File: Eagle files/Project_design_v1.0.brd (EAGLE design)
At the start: 57.5 x 43.2 mm, 64 parts, among them CN1 USB_CONN, CN2 BATT_IN_JST, IC1 TPS73233DBVT, IC2 TPS73233DBVT, IC3 MCP73833T-AMI/MF, IC4 STM32F042K6T6, IC5 MCP9700T-E/TT, IC6 TLV379IDBVT, Q1 PMV16XN, Q2 PMV16XN, Q3 PMV16XN, Q4 PMV16XN

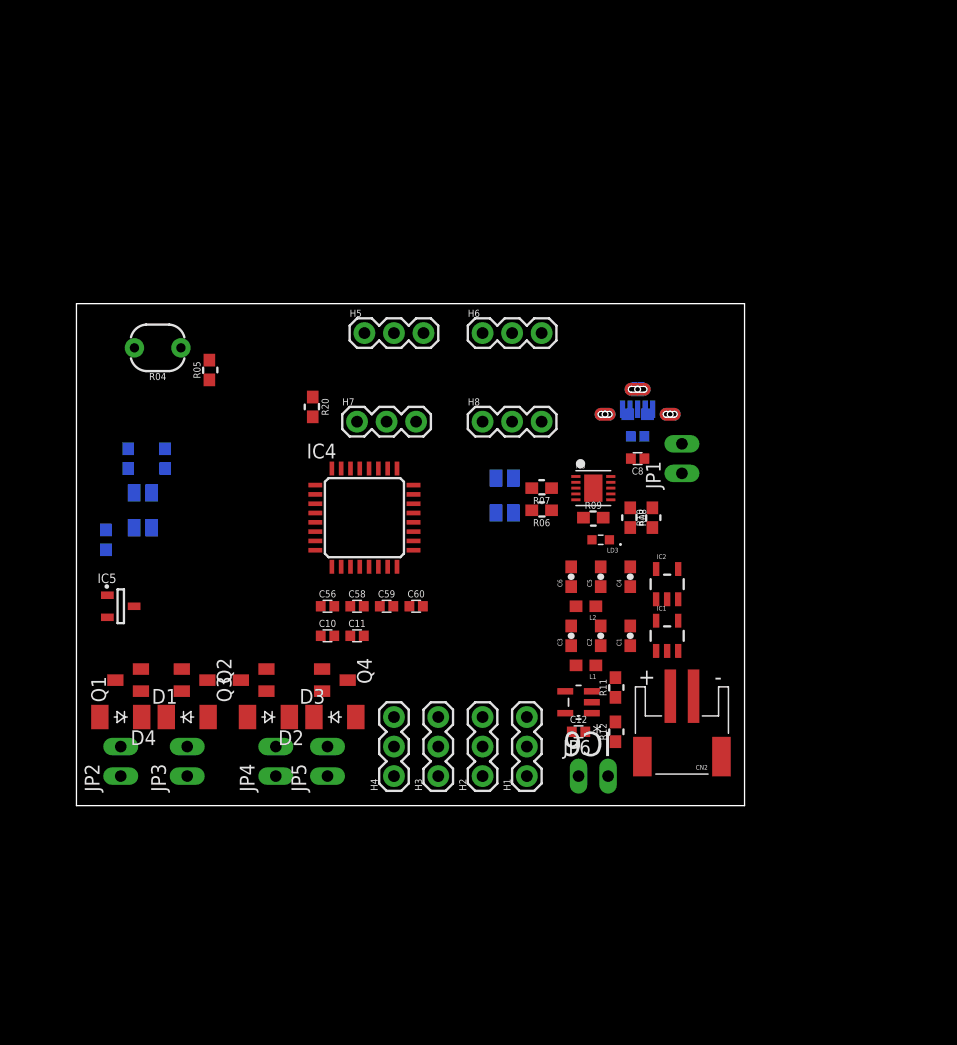
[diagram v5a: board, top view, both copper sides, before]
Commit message: schematic almose finished, part number edited, and PIR & buzzer added
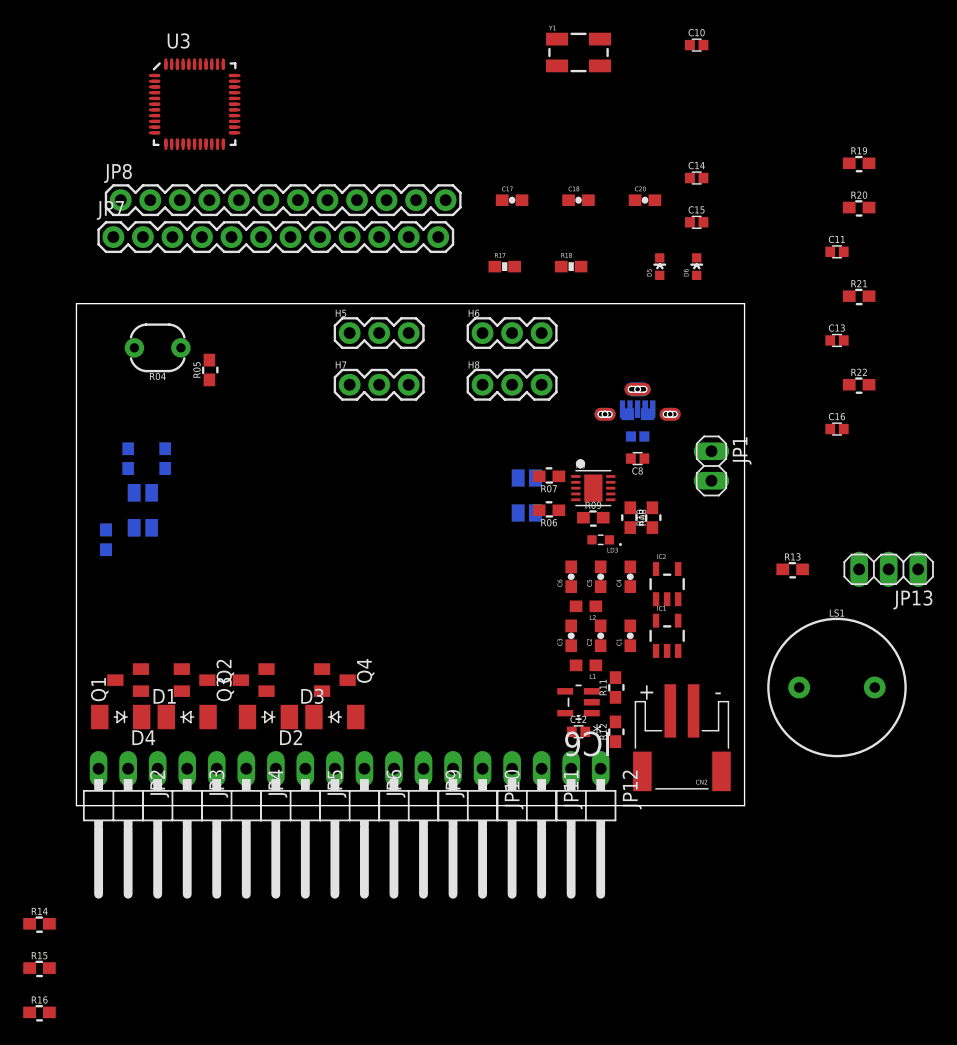
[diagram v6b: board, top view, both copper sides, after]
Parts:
- removed C56, C58, C59, C60: 100n, custom_part:0402
- removed H1, H2, H3, H4: SOIL_MOISTURE, potentiometer:SOIL_MOISTURE
- removed IC4: STM32F042K6T6, stm32-microcontrollers:LQFP32-7X7
- removed IC5: MCP9700T-E/TT, MCP9700T-E_TT:SOT95P237X112-3N
- added C13, C14, C15, C16: 100n, custom_part:0402
- added C17, C18: 22pF, SparkFun:0603-CAP
- added C20: 1uF, SparkFun:0603-CAP
- added D5: Green, SparkFun:LED-0603
- added D6: Yellow, SparkFun:LED-0603
- added JP10, JP11, JP12, JP9: Connectors, pinhead:1X02/90
- added JP13: PIN-1X3, pinhead:1X03
- added JP7, JP8: (no value), SparkFun:1X12
- added LS1: BUZZER-PTH_KIT, SparkFun-Electromechanical:BUZZER-12MM-KIT
- added R13, R15, R16: 330, custom_part:0603
- added R14, R19, R21, R22: 10k, custom_part:0603
- added R17, R18: 22, SparkFun:0603-RES
- added U3: ATMEGA32U4, Testing:QFN-44-NOPAD_1:1-OUTFAKES
- added Y1: 16MHz, SparkFun:CRYSTAL-SMD-5X3
- JP1: value Contact_pin -> Connectors; device microbuilder:1X02_OVAL -> pinhead:1X02
- JP2, JP3, JP4, JP5, JP6: value Contact_pin -> Connectors; device microbuilder:1X02_OVAL -> pinhead:1X02/90
- R06, R07, R08: value 221 -> 330
- R11, R12: value 221 -> 10k
- moved C10 59.9 mm to (53.3, 65.4)
- moved C11 52.9 mm to (65.4, 47.6)
- moved R20 50.0 mm to (67.3, 51.4), turned to 0 degrees
- moved JP6 21.2 mm to (23.5, -0.64), turned to 180 degrees
- moved JP4 5.85 mm to (13.3, -0.64), turned to 180 degrees
- moved JP5 5.46 mm to (18.4, -0.64), turned to 180 degrees
- moved JP3 4.62 mm to (8.26, -0.64), turned to 180 degrees
- moved JP2 4.49 mm to (3.17, -0.64), turned to 180 degrees
- moved H7 3.24 mm to (26.0, 36.2)
- moved H8 3.17 mm to (37.5, 36.2)
- moved JP1 2.62 mm to (54.6, 29.2), turned to 270 degrees
- moved LD2 1.91 mm to (38.7, 26.7)
- moved CN2 1.27 mm to (52.1, 4.45)
- moved H5 1.27 mm to (26.0, 40.6)
- moved R07 1.20 mm to (40.6, 28.3)
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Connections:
- removed net BOOT0: IC4.31, R20.2
- removed net CHARGE_CMD: IC4.11
- removed net CTRL_MOIST1: H1.1
- removed net CTRL_MOIST2: H2.1
- removed net CTRL_MOIST3: H3.1
- removed net CTRL_MOIST4: H4.1
- removed net DAC_CLK: IC4.12
- removed net DAC_D2: IC4.13
- removed net DAC_D3: IC4.18
- removed net DAC_D4: IC4.19
- removed net DAC_D5: IC4.20
- removed net DAC_D6: IC4.21
- removed net DAC_D7: IC4.22
- removed net DAC_D8: IC4.25
- removed net HV_DONE: IC4.10
- removed net LI_PRESET: IC4.2
- removed net LOAD_CURRENT_1: IC4.6
- removed net LOAD_CURRENT_2: IC4.7
- removed net LOAD_CURRENT_3: IC4.8
- removed net LOAD_CURRENT_4: IC4.9
- removed net MUX_DIS: IC4.28
- removed net MUX_IN: IC4.14
- removed net MUX_S0: IC4.15
- removed net MUX_S1: IC4.26
- removed net MUX_S2: IC4.27
- removed net NRST: C59.1, IC4.4
- removed net SWCLK: IC4.24
- removed net SWDIO: IC4.23
- removed net TEMP_READ: IC5.2
- removed net USART1_RX/I2C1_SDA: IC4.30
- removed net USART1_TX/I2C1_SCL: IC4.29
- new net A0: JP7.8, U3.36
- new net A1: JP7.7, U3.37
- new net A2: JP7.6, U3.38
- new net A3: JP7.5, U3.39
- new net A4: U3.40
- new net A5: U3.41
- new net ALARM: JP13.3
- new net AREF: U3.42
- new net BUZZ: LS1.+
- new net D+: R17.1, U3.4
- new net D-: R18.1, U3.3
- new net D10: JP7.12, U3.30
- new net D11: U3.12
- new net D12: U3.26
- new net D13: U3.32
- new net D14: U3.8
- new net D2: JP8.8, U3.19
- new net D3: JP8.7, U3.18
- new net D4: JP8.6, U3.25
- new net D5: JP8.5, U3.31
- new net D6: JP8.4, U3.27
- new net D7: JP8.3, U3.1
- new net D8: JP8.2, U3.28
- new net D9: JP8.1, U3.29
- new net MISO: JP7.10, U3.11
- new net MOSI: JP7.11, U3.10
- new net N$18: C17.1, U3.17, Y1.3
- new net N$19: C20.2, U3.6
- new net N$20: CN1.2, R18.2
- new net N$21: CN1.3, R17.2
- new net N$22: LS1.-, R13.1
- new net N$23: D6.C
- new net N$24: D5.C
- new net N$9: C18.1, U3.16, Y1.1
- new net RESET: JP7.3, U3.13
- new net RXI: JP8.11, U3.20
- new net SCK: JP7.9, U3.9
- new net TXLED: U3.22
- new net TXO: JP8.12, U3.21
- net 3.3V: now also JP13.1, R19.2, R20.2, R21.2, R22.2, U3.14, U3.24, U3.34, U3.44; no longer C10.1, C11.1, C56.1, C58.1, IC4.1, IC4.17, IC5.1
- net 5.0V: now also U3.2, U3.7
- net GND: now also C13.2, C15.2, C16.2, C17.2, C18.2, C20.1, JP10.2, JP11.2, JP12.2, JP13.2, JP7.1, JP7.2, JP8.10, JP8.9, JP9.2, R13.2, U3.15, U3.23, U3.33, U3.35, U3.43, U3.5; no longer C10.2, C56.2, C58.2, C59.2, C60.2, H1.2, H2.2, H3.2, H4.2, IC4.16, IC4.32, IC5.3, R20.1
- net LED_G: no longer IC4.3
- net LEVEL_SENSOR: now also JP12.1; no longer JP6.1
- net MOISTURE1: now also C15.1, JP6.1, R19.1; no longer H1.3
- net MOISTURE2: now also C11.1, JP9.1, R20.1; no longer H2.3
- net MOISTURE3: now also C13.1, JP11.1, R21.1; no longer H3.3
- net MOISTURE4: now also C16.1, JP10.1, R22.1; no longer H4.3
- net VCC: now also D5.A, D6.A, JP7.4; no longer C60.1, IC4.5

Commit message: schematics design uptaded and adjusted for exportation for the MS2
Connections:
- net 3.3V: now also C10.1, R14.2
- net GND: now also C10.2
- net RESET: now also R14.1
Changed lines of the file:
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@@
 <contactref element="U3" pad="24"/>
 <contactref element="U3" pad="44"/>
+<contactref element="R14" pad="2"/>
+<contactref element="C10" pad="1"/>
 <wire x1="68.16" y1="51.435" x2="68.16" y2="55.245" width="0" layer="19" extent="1-1"/>
 <wire x1="68.16" y1="43.815" x2="68.16" y2="51.435" width="0" layer="19" extent="1-1"/>
 <wire x1="68.16" y1="36.195" x2="68.16" y2="43.815" width="0" layer="19" extent="1-1"/>
 <wire x1="72.39" y1="20.32" x2="68.16" y2="36.195" width="0" layer="19" extent="1-1"/>
+<wire x1="52.76" y1="65.405" x2="68.16" y2="55.245" width="0" layer="19" extent="1-1"/>
 <wire x1="42.965" y1="17.145" x2="72.39" y2="20.32" width="0" layer="19" extent="1-1"/>
 <wire x1="42.545" y1="18.835" x2="42.965" y2="17.145" width="0" layer="19" extent="1-1"/>
@@
 <wire x1="7.695" y1="63.6615" x2="12.625" y2="63.6615" width="0" layer="19" extent="1-1"/>
 <wire x1="6.465" y1="23.9" x2="23.495" y2="36.195" width="0" layer="19" extent="16-16"/>
+<wire x1="-2.325" y1="-10.16" x2="6.465" y2="23.9" width="0" layer="19" extent="1-16"/>
 </signal>
 <signal name="N$34">
@@
 <contactref element="JP11" pad="2"/>
 <contactref element="JP7" pad="1"/>
-<wire x1="65.985" y1="40.005" x2="65.985" y2="47.625" width="0" layer="19" extent="1-1"/>
-<wire x1="65.985" y1="32.385" x2="65.985" y2="40.005" width="0" layer="19" extent="1-1"/>
-<wire x1="54.61" y1="30.48" x2="65.985" y2="32.385" width="0" layer="19" extent="1-1"/>
-<wire x1="51.82" y1="33.655" x2="54.61" y2="30.48" width="0" layer="19" extent="16-16"/>
-<wire x1="49.56" y1="34.095" x2="51.82" y2="33.655" width="0" layer="19" extent="16-16"/>
-<wire x1="49.24" y1="35.795" x2="49.56" y2="34.095" width="0" layer="19" extent="16-16"/>
-<wire x1="47.41" y1="33.655" x2="49.56" y2="34.095" width="0" layer="19" extent="16-16"/>
-<wire x1="46.17" y1="33.655" x2="47.41" y2="33.655" width="0" layer="19" extent="16-16"/>
+<contactref element="C10" pad="2"/>
+<wire x1="48.045" y1="52.07" x2="53.92" y2="65.405" width="0" layer="19" extent="1-1"/>
+<wire x1="44.03" y1="52.07" x2="48.045" y2="52.07" width="0" layer="19" extent="1-1"/>
+<wire x1="38.315" y1="52.07" x2="44.03" y2="52.07" width="0" layer="19" extent="1-1"/>
+<wire x1="53.92" y1="50.165" x2="48.045" y2="52.07" width="0" layer="19" extent="1-1"/>
+<wire x1="37.465" y1="40.64" x2="38.315" y2="52.07" width="0" layer="19" extent="1-1"/>
+<wire x1="37.465" y1="36.195" x2="37.465" y2="40.64" width="0" layer="19" extent="1-1"/>
+<wire x1="46.17" y1="33.655" x2="37.465" y2="36.195" width="0" layer="19" extent="16-16"/>
+<wire x1="47.41" y1="33.655" x2="46.17" y2="33.655" width="0" layer="19" extent="16-16"/>
 <wire x1="47.68" y1="31.75" x2="47.41" y2="33.655" width="0" layer="19" extent="16-16"/>
 <wire x1="47.68" y1="29.845" x2="47.68" y2="31.75" width="0" layer="19" extent="1-16"/>
+<wire x1="49.56" y1="34.095" x2="47.41" y2="33.655" width="0" layer="19" extent="16-16"/>
+<wire x1="49.24" y1="35.795" x2="49.56" y2="34.095" width="0" layer="19" extent="16-16"/>
+<wire x1="51.82" y1="33.655" x2="49.56" y2="34.095" width="0" layer="19" extent="16-16"/>
+<wire x1="54.61" y1="30.48" x2="51.82" y2="33.655" width="0" layer="19" extent="16-16"/>
 <wire x1="42.95" y1="26.305" x2="47.68" y2="29.845" width="0" layer="19" extent="1-1"/>
 <wire x1="43.6" y1="24.765" x2="42.95" y2="26.305" width="0" layer="19" extent="1-1"/>
@@
 <wire x1="9.06" y1="9.845" x2="16.34" y2="11.745" width="0" layer="19" extent="1-1"/>
 <wire x1="5.545" y1="11.745" x2="9.06" y2="9.845" width="0" layer="19" extent="1-1"/>
-<wire x1="37.465" y1="36.195" x2="46.17" y2="33.655" width="0" layer="19" extent="16-16"/>
-<wire x1="37.465" y1="40.64" x2="37.465" y2="36.195" width="0" layer="19" extent="1-1"/>
 <wire x1="26.035" y1="40.64" x2="37.465" y2="40.64" width="0" layer="19" extent="1-1"/>
 <wire x1="26.035" y1="36.195" x2="26.035" y2="40.64" width="0" layer="19" extent="1-1"/>
-<wire x1="38.315" y1="52.07" x2="37.465" y2="40.64" width="0" layer="19" extent="1-1"/>
-<wire x1="44.03" y1="52.07" x2="38.315" y2="52.07" width="0" layer="19" extent="1-1"/>
-<wire x1="48.045" y1="52.07" x2="44.03" y2="52.07" width="0" layer="19" extent="1-1"/>
-<wire x1="53.92" y1="50.165" x2="48.045" y2="52.07" width="0" layer="19" extent="1-1"/>
 <wire x1="26.67" y1="52.07" x2="26.035" y2="40.64" width="0" layer="19" extent="1-1"/>
 <wire x1="24.13" y1="52.07" x2="26.67" y2="52.07" width="0" layer="19" extent="1-1"/>
+<wire x1="65.985" y1="32.385" x2="54.61" y2="30.48" width="0" layer="19" extent="1-1"/>
+<wire x1="65.985" y1="40.005" x2="65.985" y2="32.385" width="0" layer="19" extent="1-1"/>
+<wire x1="65.985" y1="47.625" x2="65.985" y2="40.005" width="0" layer="19" extent="1-1"/>
 <wire x1="13.9895" y1="57.86" x2="24.13" y2="52.07" width="0" layer="19" extent="1-1"/>
 <wire x1="9.174" y1="56.9885" x2="13.4965" y2="57.86" width="0" layer="19" extent="1-1"/>
@@
 <contactref element="JP7" pad="3"/>
 <contactref element="U3" pad="13"/>
+<contactref element="R14" pad="1"/>
 <wire x1="8.255" y1="48.895" x2="8.188" y2="56.4955" width="0" layer="19" extent="1-1"/>
+<wire x1="-4.025" y1="-10.16" x2="8.255" y2="48.895" width="0" layer="19" extent="1-1"/>
 </signal>
 <signal name="SCK">
